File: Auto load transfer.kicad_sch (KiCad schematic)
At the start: 20 parts

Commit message: Added some decoupling
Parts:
- added C? (x2): 100n, symbol Device:C_Small
- added C?: 470u, symbol Device:C_Polarized_Small
- added C? (x2): 10n, symbol Device:C_Small
- added F? (x2): Fuse, symbol Device:Fuse
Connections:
- net +5V: now also C?.1, C?.1, C?.1, C?.1, C?.1
- net GND: now also C?.2, C?.2, C?.2, C?.2, C?.2
- net at J?.1 (AC/L), K?.4 (24_NO), R?.1: now also F?.2; no longer J?.1 (Pin_1)
- net at J?.1 (AC/L), K?.2 (22_NC), R?.2: now also F?.2; no longer J?.1 (Pin_1)
- new net: F?.1, J?.1 (Pin_1) (x2)
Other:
- moved on the sheet: D?, IC?, J?, R?

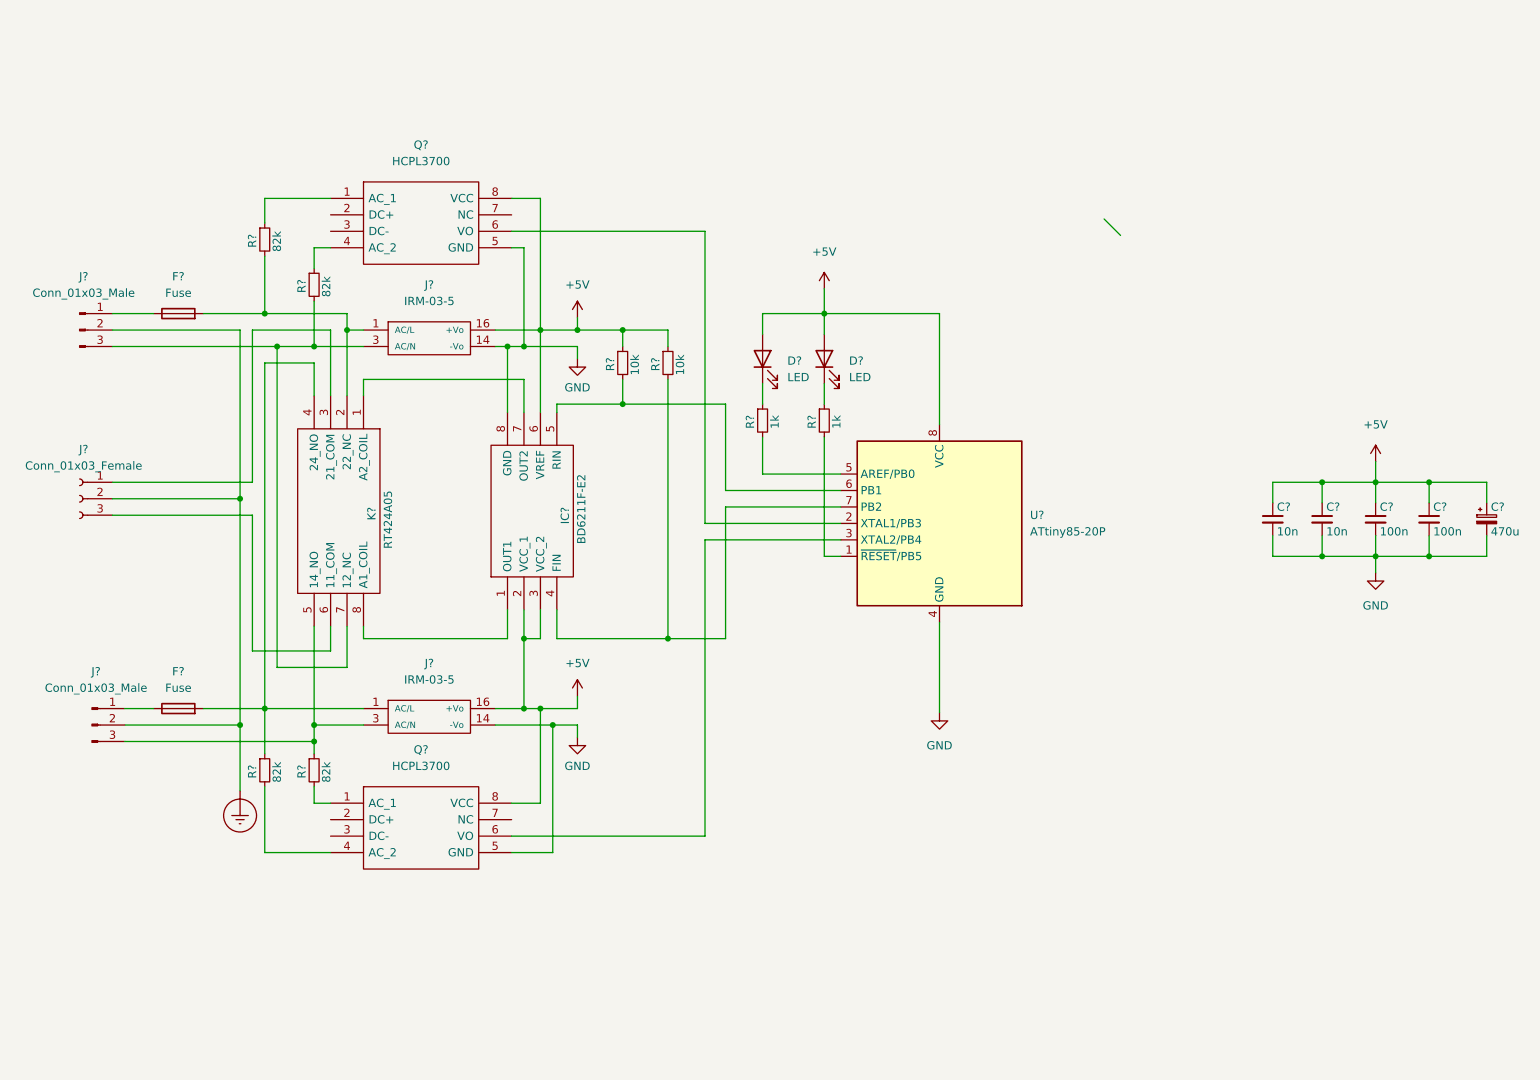
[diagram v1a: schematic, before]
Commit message: Change to Arduino based block diagram
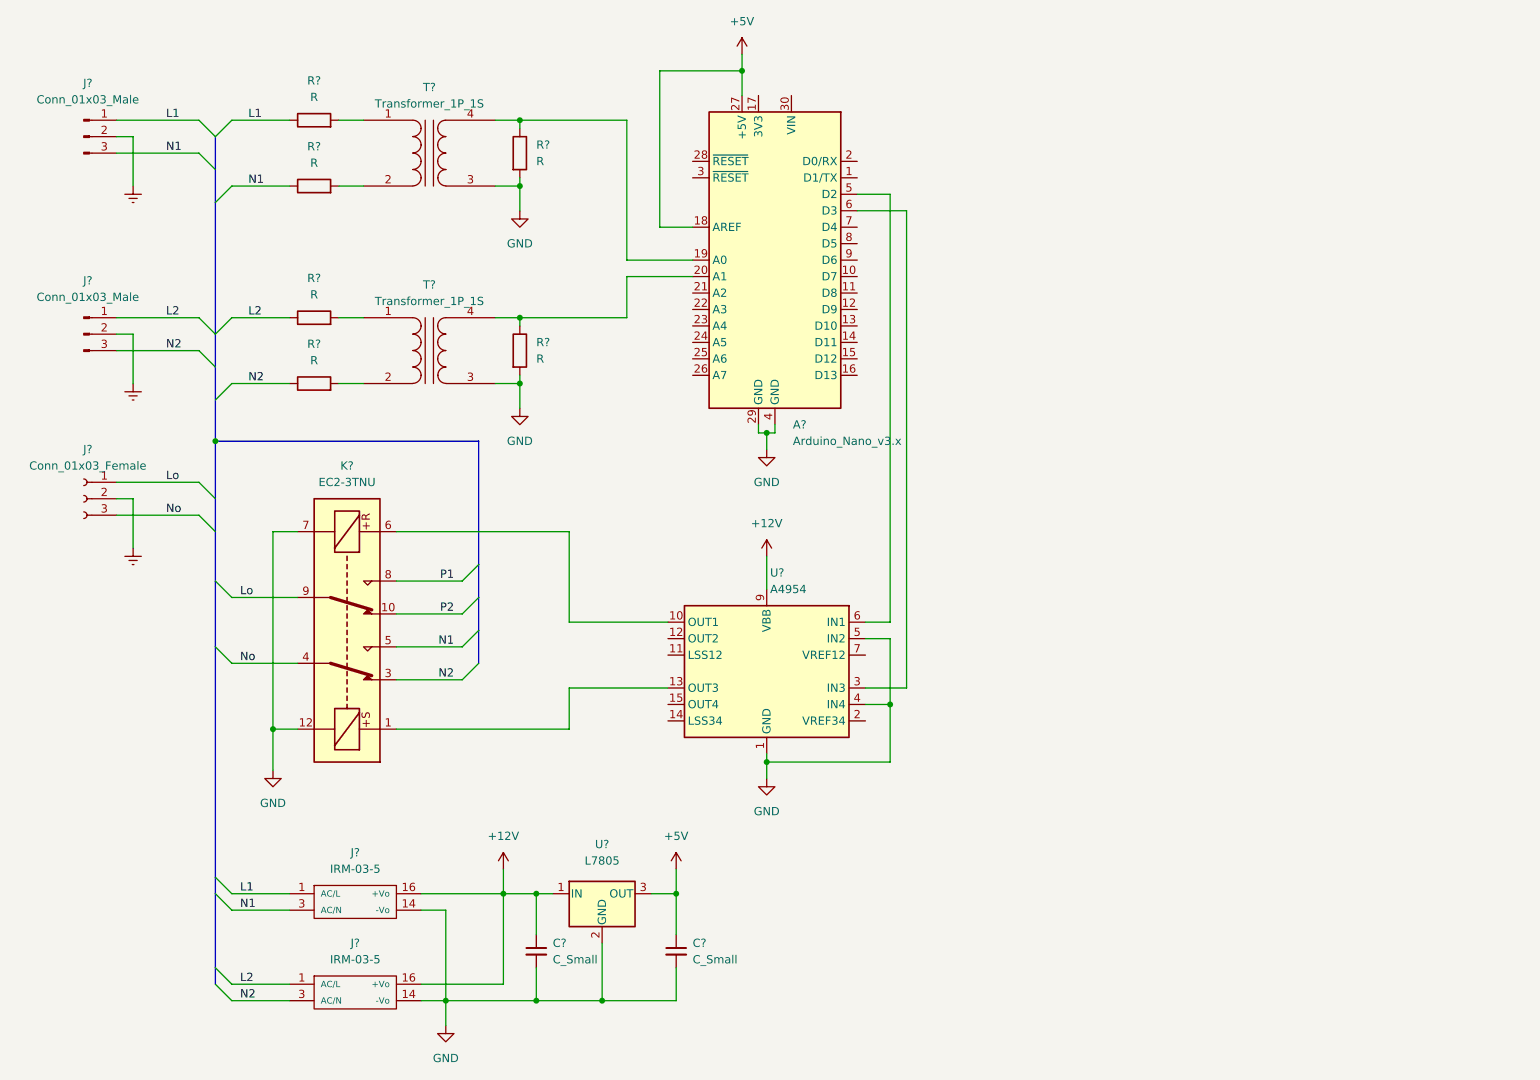
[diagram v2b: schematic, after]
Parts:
- removed C? (x2): 100n, symbol Device:C_Small
- removed C?: 470u, symbol Device:C_Polarized_Small
- removed C? (x2): 10n, symbol Device:C_Small
- removed D? (x2): LED, symbol Device:LED
- removed F? (x2): Fuse, symbol Device:Fuse
- removed IC?: BD6211F-E2, SOIC127P620X160-8N, symbol SamacSys_Parts:BD6211F-E2
- removed J? (x2): Conn_01x03_Male, symbol Connector:Conn_01x03_Male
- removed J?: Conn_01x03_Female, symbol Connector:Conn_01x03_Female
- removed J? (x2): IRM-03-5, symbol miscellaneous:IRM-03-5
- removed K?: RT424A05, RT42, symbol SamacSys_Parts:RT424A05
- removed Q? (x2): HCPL3700, DIP762W56P254L966H508Q8N, symbol SamacSys_Parts:HCPL3700
- removed R? (x2): 1k, symbol Device:R_Small
- removed R? (x2): 10k, symbol Device:R_Small
- removed R? (x4): 82k, symbol Device:R_Small
- removed U?: ATtiny85-20P, Package_DIP:DIP-8_W7.62mm, symbol MCU_Microchip_ATtiny:ATtiny85-20P
- added A?: Arduino_Nano_v3.x, Module:Arduino_Nano, symbol MCU_Module:Arduino_Nano_v3.x
- added C? (x2): C_Small, symbol Device:C_Small
- added J? (x2): Conn_01x03_Male, symbol Connector:Conn_01x03_Male
- added J? (x2): IRM-03-5, symbol miscellaneous:IRM-03-5
- added J?: Conn_01x03_Female, symbol Connector:Conn_01x03_Female
- added K?: EC2-3TNU, Relay_THT:Relay_DPDT_Kemet_EC2_DoubleCoil, symbol Relay:EC2-3TNU
- added R? (x6): R, symbol Device:R
- added T? (x2): Transformer_1P_1S, symbol Device:Transformer_1P_1S
- added U?: L7805, symbol Regulator_Linear:L7805
- added U?: A4954, Package_SO:TSSOP-16-1EP_4.4x5mm_P0.65mm_EP3x3mm, symbol Driver_Motor:A4954
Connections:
- net +5V: now also A?.18 (AREF), A?.27 (+5V), C?.1, U?.3 (OUT)
- net GND: now also A?.29 (GND), A?.4 (GND), C?.2, C?.2, J?.14 (-Vo), J?.14 (-Vo), K?.12, K?.7, R?.2, R?.2, T?.3 (SA), T?.3 (SA), U?.1 (GND), U?.17 (GND), U?.2 (GND), U?.4 (IN4), U?.5 (IN2), U?.8 (GND)
- new net: R?.2, T?.1 (AA) (x2)
- new net: A?.20 (A1), R?.1, T?.4 (SB)
- new net: R?.2, T?.2 (AB) (x2)
- new net: A?.19 (A0), R?.1, T?.4 (SB)
- new net: A?.5 (D2), U?.6 (IN1)
- new net: A?.6 (D3), U?.3 (IN3)
- new net: K?.1, U?.13 (OUT3)
- new net: K?.6, U?.10 (OUT1)
- new net +12V: C?.1, J?.16 (+Vo), J?.16 (+Vo), U?.1 (IN), U?.16 (VBB), U?.9 (VBB)
- new net Earth: J?.2 (Pin_2), J?.2 (Pin_2), J?.2 (Pin_2)
- new net L1: J?.1 (AC/L), J?.1 (Pin_1), R?.1
- new net L2: J?.1 (AC/L), J?.1 (Pin_1), R?.1
- new net Lo: J?.1 (Pin_1), K?.9
- new net N1: J?.3 (AC/N), J?.3 (Pin_3), K?.5, R?.1
- new net N2: J?.3 (AC/N), J?.3 (Pin_3), K?.3, R?.1
- new net No: J?.3 (Pin_3), K?.4
- new net P1: K?.8
- new net P2: K?.10

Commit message: Prepare for PCB layout
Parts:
- removed K?: EC2-3TNU, Relay_THT:Relay_DPDT_Kemet_EC2_DoubleCoil, symbol Relay:EC2-3TNU
- removed R? (x2): R, symbol Device:R
- removed T? (x2): Transformer_1P_1S, symbol Device:Transformer_1P_1S
- removed U?: A4954, Package_SO:TSSOP-16-1EP_4.4x5mm_P0.65mm_EP3x3mm, symbol Driver_Motor:A4954
- added D? (x2): 1n4148, symbol Device:D
- added D? (x2): LED, symbol Device:LED
- added J? (x2): AC1, symbol Connector:Conn_01x01_Female
- added J?: L298N-O, symbol Connector:Conn_01x04_Female
- added J?: L298N-P, symbol Connector:Conn_01x02_Female
- added J? (x2): ZMPT101B, symbol Connector:Conn_01x04_Female
- added J? (x2): AC2, symbol Connector:Conn_01x01_Female
- added J?: L298N-I, symbol Connector:Conn_01x04_Female
- added K?: RT424F12, RT424F12, symbol SamacSys_Parts:RT424F12
- added R? (x2): 470, symbol Device:R
- added SW?: SW_Push, symbol Switch:SW_Push
- J? (x2): value IRM-03-5 -> IRM-03-12
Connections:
- net +12V: now also J?.1 (Pin_1)
- net +5V: now also D?.2 (A), D?.2 (A), J?.1 (Pin_1), J?.1 (Pin_1)
- net GND: now also D?.2 (A), D?.2 (A), J?.2 (Pin_2), J?.2 (Pin_2), J?.3 (Pin_3), J?.3 (Pin_3), J?.4 (Pin_4), J?.4 (Pin_4), J?.4 (Pin_4), K?.2 (A2), SW?.2
- net L1: now also K?.9 (22)
- net L2: now also K?.7 (24)
- net Lo: now also K?.8 (21)
- net N1: now also K?.4 (12); no longer R?.1
- net N2: now also K?.6 (14); no longer R?.1
- net No: now also K?.5 (11)
- net at R?.2: now also J?.1 (Pin_1) (x4)
- net at A?.20 (A1): now also J?.2 (Pin_2)
- net at A?.19 (A0): now also J?.2 (Pin_2)
- net at A?.5 (D2): now also J?.1 (Pin_1)
- net at A?.6 (D3): now also J?.3 (Pin_3)
- net at A?.7 (D4): now also R?.1
- net at A?.8 (D5): now also R?.1
- net at A?.9 (D6): now also SW?.1
- new net: D?.1 (K), J?.4 (Pin_4), K?.1 (A1)
- new net: D?.1 (K), R?.2 (x2)
- new net: D?.1 (K), J?.1 (Pin_1), K?.3 (A3)
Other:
- moved on the sheet: R?

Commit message: PCB layout beginning
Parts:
- C1, C2: renamed from C?; footprint (none) -> Capacitor_THT:C_Disc_D5.0mm_W2.5mm_P5.00mm
- D1, D2: renamed from D?; footprint (none) -> Diode_THT:D_DO-35_SOD27_P7.62mm_Horizontal; symbol Device:D -> Diode:1N4148
- D3, D4: renamed from D?; footprint (none) -> TerminalBlock:TerminalBlock_bornier-2_P5.08mm
- J1, J2, J3: renamed from J?; footprint (none) -> TerminalBlock:TerminalBlock_bornier-3_P5.08mm
- J10, J11, J12, J14: renamed from J?; footprint (none) -> Connector_PinHeader_2.54mm:PinHeader_1x04_P2.54mm_Vertical
- J13: renamed from J?; footprint (none) -> Connector_PinHeader_2.54mm:PinHeader_1x02_P2.54mm_Vertical
- J4, J5: renamed from J?; footprint (none) -> Miscellaneous:MeanWell_IRM
- J6: renamed from J?; value AC1 -> ACL1; footprint (none) -> MountingHole:MountingHole_2.2mm_M2_DIN965_Pad
- J7: renamed from J?; value AC2 -> ACN1; footprint (none) -> MountingHole:MountingHole_2.2mm_M2_DIN965_Pad
- J8: renamed from J?; value AC1 -> ACL2; footprint (none) -> MountingHole:MountingHole_2.2mm_M2_DIN965_Pad
- J9: renamed from J?; value AC2 -> ACN2; footprint (none) -> MountingHole:MountingHole_2.2mm_M2_DIN965_Pad
- K1: renamed from K?; footprint RT424F12 -> SamacSys_Parts:RT424F12
- R1, R2, R3, R4, R5, R6: renamed from R?; footprint (none) -> Resistor_THT:R_Axial_DIN0309_L9.0mm_D3.2mm_P12.70mm_Horizontal
- SW1: renamed from SW?; footprint (none) -> TerminalBlock:TerminalBlock_bornier-2_P5.08mm
- U1: renamed from U?; footprint (none) -> Package_TO_SOT_THT:TO-220-3_Vertical
- gave numbers to parts that had none: 1
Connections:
- net GND: now also K1.3 (A3); no longer K1.2 (A2)
- net N2: now also R4.1
- net at D1.1 (K), J12.1 (Pin_1): now also K1.2 (A2); no longer K1.3 (A3)
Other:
- moved on the sheet: D1
